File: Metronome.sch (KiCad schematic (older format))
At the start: 30 parts, among them CON1 PDI_50mil, IC1 ATXMEGA8E5-MU, P1 USB_B, Q1 Q_PMOS_GSD, U1 AS1117, U2 NCP706A

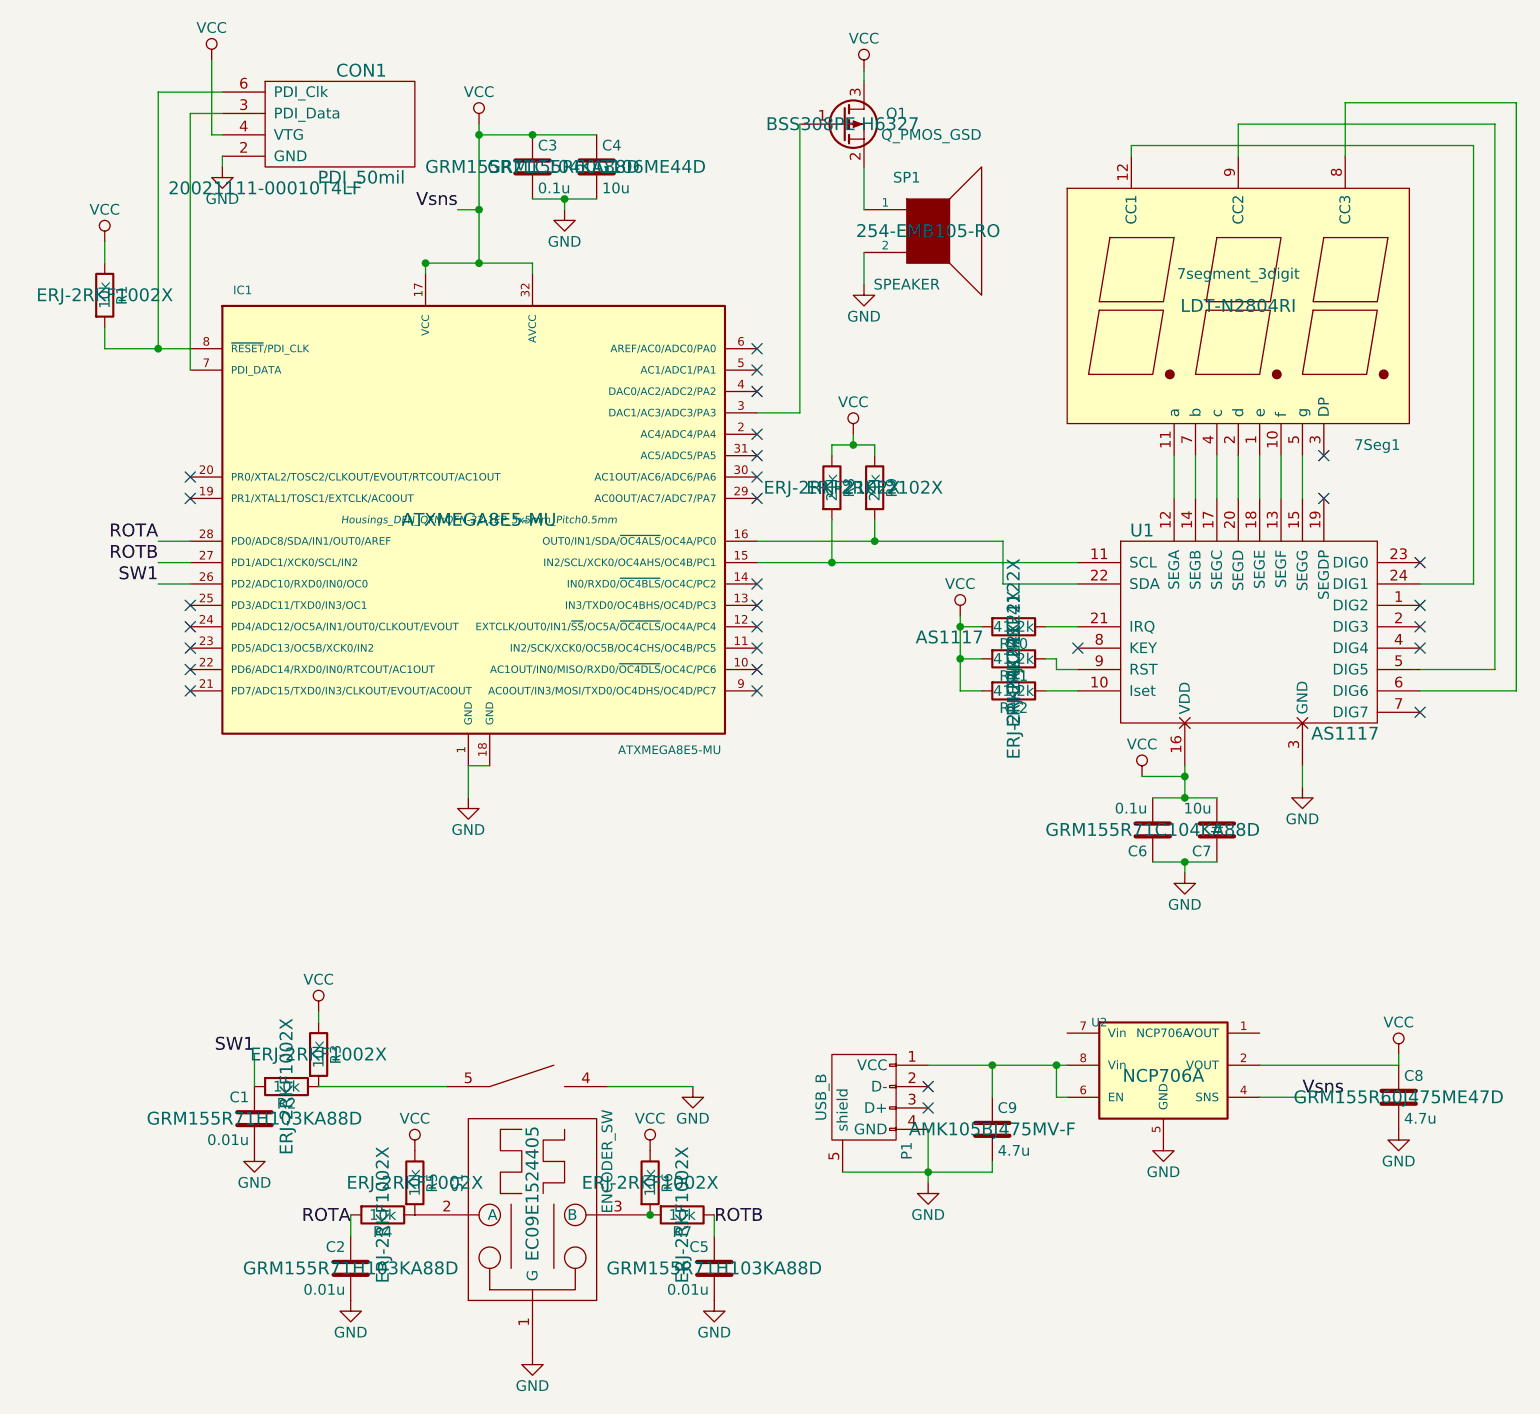
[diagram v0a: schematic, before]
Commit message: Hide footprints and MFP fields in schematic.
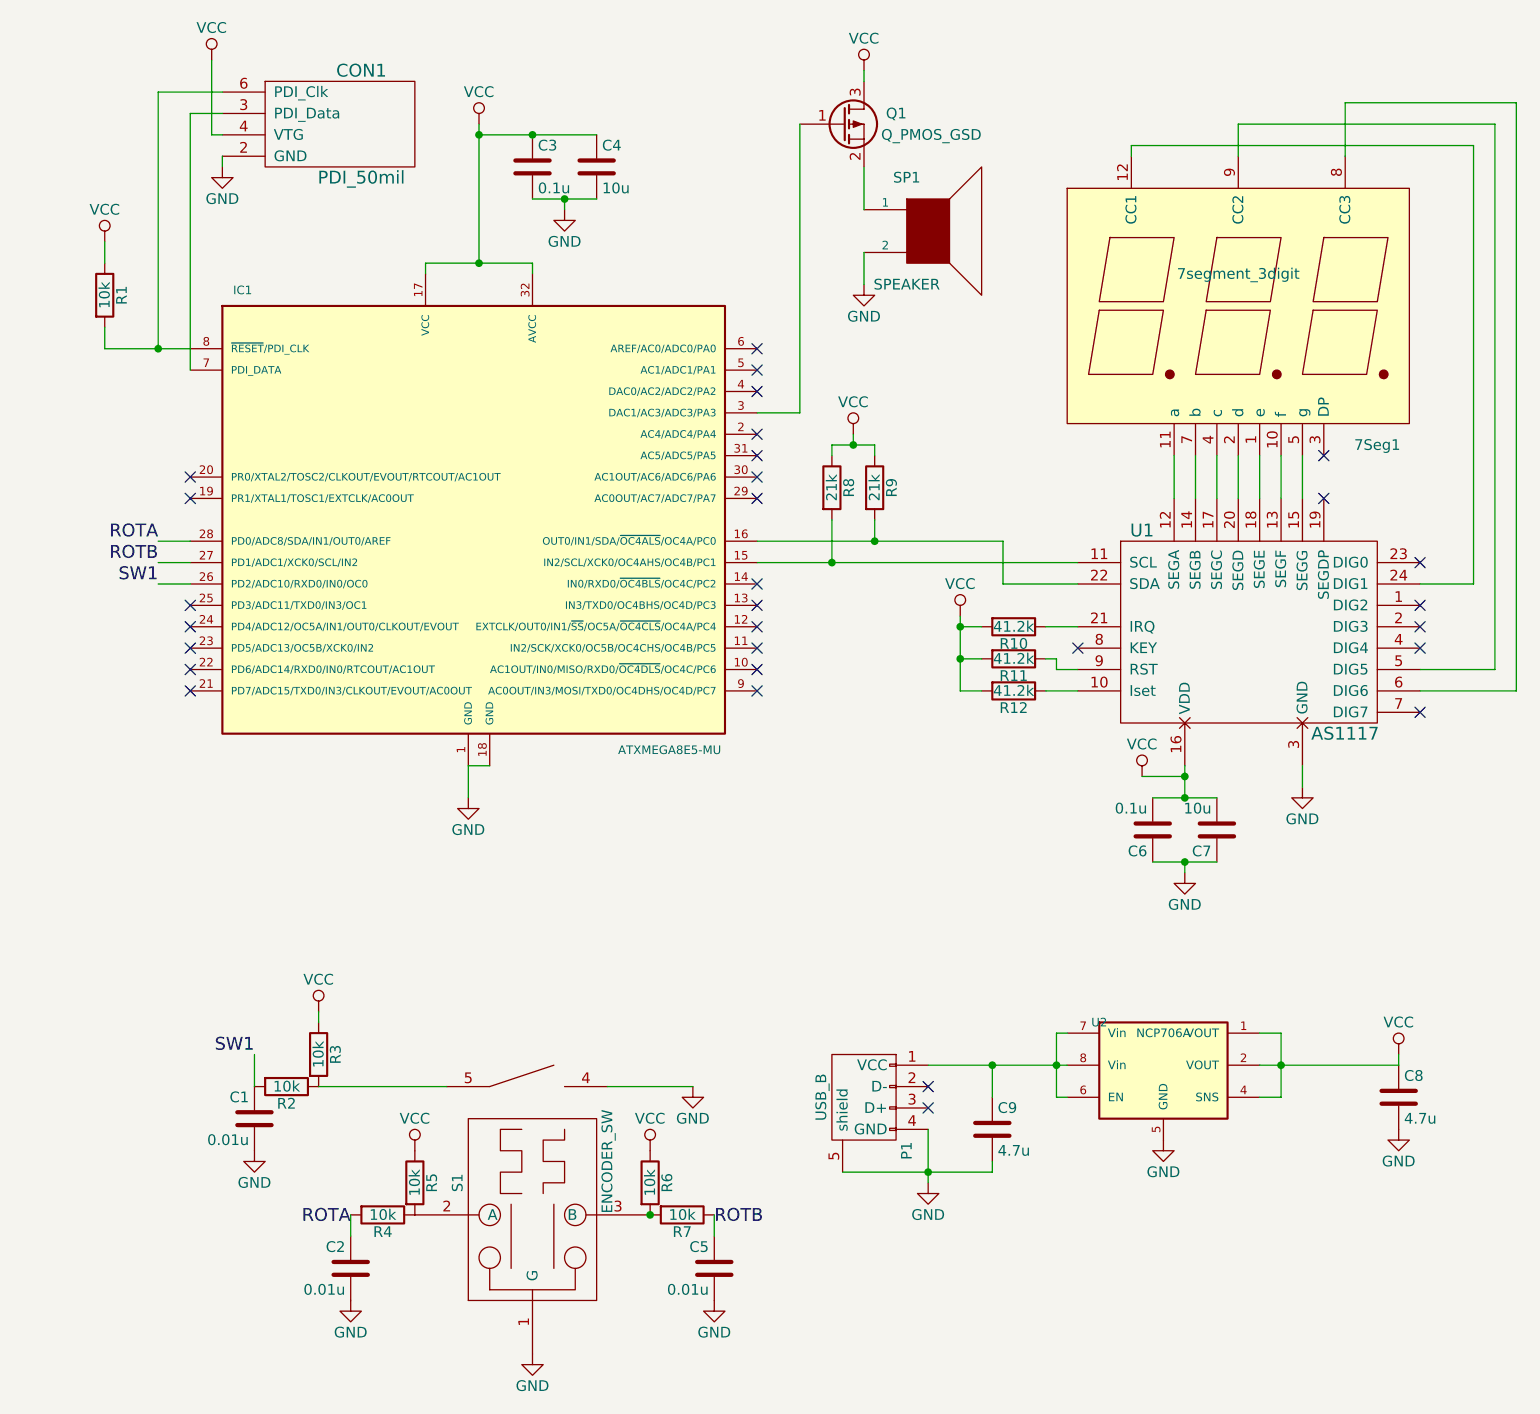
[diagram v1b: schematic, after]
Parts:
- C7: MFP # -> GRM155R60G106ME44D
- P1: MFN (none) -> FCI; MFP (none) -> 10118192-0001LF
- U1: MFP AS1117 -> AS1117-BQFT
- U2: MFP NCP706A -> NCP706AMX300TAG
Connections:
- net VCC: now also U2.1 (VOUT)
- net at C9.1, P1.1 (VCC), U2.6 (EN)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: now also U2.7 (Vin)
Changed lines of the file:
@@
 EESchema Schematic File Version 2
+LIBS:power
+LIBS:device
+LIBS:transistors
+LIBS:conn
+LIBS:linear
+LIBS:regul
+LIBS:74xx
+LIBS:cmos4000
+LIBS:adc-dac
+LIBS:memory
+LIBS:xilinx
+LIBS:microcontrollers
+LIBS:dsp
+LIBS:microchip
+LIBS:analog_switches
+LIBS:motorola
+LIBS:texas
+LIBS:intel
+LIBS:audio
+LIBS:interface
+LIBS:digital-audio
+LIBS:philips
+LIBS:display
+LIBS:cypress
+LIBS:siliconi
+LIBS:opto
+LIBS:atmel
+LIBS:contrib
+LIBS:valves
 LIBS:ams
 LIBS:encoder
@@
 LIBS:7segment_3digits
 LIBS:pdi_50mil
+LIBS:74xgxx
+LIBS:ac-dc
+LIBS:actel
+LIBS:Altera
+LIBS:analog_devices
+LIBS:brooktre
+LIBS:cmos_ieee
+LIBS:dc-dc
+LIBS:diode
+LIBS:elec-unifil
+LIBS:ESD_Protection
+LIBS:ftdi
+LIBS:gennum
+LIBS:graphic
+LIBS:hc11
+LIBS:ir
+LIBS:Lattice
+LIBS:logo
+LIBS:maxim
+LIBS:microchip_dspic33dsc
+LIBS:microchip_pic10mcu
+LIBS:microchip_pic12mcu
+LIBS:microchip_pic16mcu
+LIBS:microchip_pic18mcu
+LIBS:microchip_pic32mcu
+LIBS:motor_drivers
+LIBS:msp430
+LIBS:nordicsemi
+LIBS:nxp_armmcu
+LIBS:onsemi
+LIBS:Oscillators
+LIBS:powerint
+LIBS:Power_Management
+LIBS:pspice
+LIBS:references
+LIBS:relays
+LIBS:rfcom
+LIBS:sensors
+LIBS:silabs
+LIBS:stm8
+LIBS:stm32
+LIBS:supertex
+LIBS:switches
+LIBS:transf
+LIBS:ttl_ieee
+LIBS:video
+LIBS:Xicor
+LIBS:Zilog
 LIBS:Metronome-cache
 EELAYER 25 0
@@
 F 0 "IC1" H 1350 4250 40  0000 L BNN
 F 1 "ATXMEGA8E5-MU" H 3150 2100 40  0000 L BNN
-F 2 "Housings_DFN_QFN:QFN-32-1EP_5x5mm_Pitch0.5mm" H 2500 3200 35  0000 C CIN
+F 2 "Housings_DFN_QFN:QFN-32-1EP_5x5mm_Pitch0.5mm" H 2500 3200 35  0001 C CIN
 F 3 "" H 2500 3200 60  0000 C CNN
 F 4 "Atmel" H 2500 3200 60  0001 C CNN "MFN"
-F 5 "ATXMEGA8E5-MU" H 2500 3200 60  0000 C CNN "MFP"
+F 5 "ATXMEGA8E5-MU" H 2500 3200 60  0001 C CNN "MFP"
 	1    2500 3200
 	1    0    0    -1
@@
 F 3 "" H 750 2150 30  0000 C CNN
 F 4 "Panasonic" H 750 2150 60  0001 C CNN "MFN"
-F 5 "ERJ-2RKF1002X" H 750 2150 60  0000 C CNN "MFP"
+F 5 "ERJ-2RKF1002X" H 750 2150 60  0001 C CNN "MFP"
 	1    750  2150
 	1    0    0    -1
@@
 F 3 "" H 4700 3750 60  0000 C CNN
 F 4 "AMS" H 4700 3750 60  0001 C CNN "MFN"
-F 5 "AS1117" H 4700 3750 60  0000 C CNN "MFP"
+F 5 "AS1117-BQFT" H 4700 3750 60  0001 C CNN "MFP"
 	1    4700 3750
 	1    0    0    -1
@@
 F 3 "" H 5650 4650 60  0000 C CNN
 F 4 "Murata" H 5650 4650 60  0001 C CNN "MFN"
-F 5 "GRM155R71C104KA88D" H 5650 4650 60  0000 C CNN "MFP"
+F 5 "GRM155R71C104KA88D" H 5650 4650 60  0001 C CNN "MFP"
 	1    5650 4650
 	-1   0    0    1
@@
 F 3 "" H 5950 4650 60  0000 C CNN
 F 4 "Murata" H 5950 4650 60  0001 C CNN "MFN"
-F 5 "#" H 5950 4650 60  0000 C CNN "MFP"
+F 5 "GRM155R60G106ME44D" H 5950 4650 60  0001 C CNN "MFP"
 	1    5950 4650
 	-1   0    0    1
@@
 F 3 "" H 5000 3700 30  0000 C CNN
 F 4 "Panasonic" H 5000 3700 60  0001 C CNN "MFN"
-F 5 "ERJ-2RKF4122X" H 5000 3700 60  0000 C CNN "MFP"
+F 5 "ERJ-2RKF4122X" H 5000 3700 60  0001 C CNN "MFP"
 	1    5000 3700
 	0    1    1    0
@@
 F 3 "" H 2750 1550 60  0000 C CNN
 F 4 "Murata" H 2750 1550 60  0001 C CNN "MFN"
-F 5 "GRM155R71C104KA88D" H 2750 1550 60  0000 C CNN "MFP"
+F 5 "GRM155R71C104KA88D" H 2750 1550 60  0001 C CNN "MFP"
 	1    2750 1550
 	1    0    0    -1
@@
 F 3 "" H 3050 1550 60  0000 C CNN
 F 4 "Murata" H 3050 1550 60  0001 C CNN "MFN"
-F 5 "GRM155R60G106ME44D" H 3050 1550 60  0000 C CNN "MFP"
+F 5 "GRM155R60G106ME44D" H 3050 1550 60  0001 C CNN "MFP"
 	1    3050 1550
 	1    0    0    -1
@@
 F 3 "" H 4150 3050 30  0000 C CNN
 F 4 "Panasonic" H 4150 3050 60  0001 C CNN "MFN"
-F 5 "ERJ-2RKF2102X" H 4150 3050 60  0000 C CNN "MFP"
+F 5 "ERJ-2RKF2102X" H 4150 3050 60  0001 C CNN "MFP"
 	1    4150 3050
 	1    0    0    -1
@@
 Wire Wire Line
 	2750 2000 2750 2050
-Connection ~ 2250 2000
 Wire Wire Line
 	2500 1400 3050 1400
@@
 F 3 "" H 2750 6350 60  0000 C CNN
 F 4 "Alps" H 2750 6350 60  0001 C CNN "MFN"
-F 5 "EC09E1524405" H 2750 6350 60  0000 C CNN "MFP"
+F 5 "EC09E1524405" H 2750 6350 60  0001 C CNN "MFP"
 	1    2750 6350
 	0    -1   -1   0
@@
 F 3 "" H 1450 6000 60  0000 C CNN
 F 4 "Murata" H 1450 6000 60  0001 C CNN "MFN"
-F 5 "GRM155R71H103KA88D" H 1450 6000 60  0000 C CNN "MFP"
+F 5 "GRM155R71H103KA88D" H 1450 6000 60  0001 C CNN "MFP"
 	1    1450 6000
 	-1   0    0    -1
@@
 F 3 "" H 5700 5800 60  0000 C CNN
 F 4 "On Semiconductor" H 5700 5800 60  0001 C CNN "MFN"
-F 5 "NCP706A" H 5700 5800 60  0000 C CNN "MFP"
+F 5 "NCP706AMX300TAG" H 5700 5800 60  0001 C CNN "MFP"
 	1    5700 5800
 	1    0    0    -1
@@
 F 3 "" H 6800 5900 60  0000 C CNN
 F 4 "Murata" H 6800 5900 60  0001 C CNN "MFN"
-F 5 "GRM155R60J475ME47D" H 6800 5900 60  0000 C CNN "MFP"
+F 5 "GRM155R60J475ME47D" H 6800 5900 60  0001 C CNN "MFP"
 	1    6800 5900
 	1    0    0    -1
@@
 F 3 "" H 5800 2200 60  0000 C CNN
 F 4 "Lumex" H 6050 2200 60  0001 C CNN "MFN"
-F 5 "LDT-N2804RI" H 6050 2200 60  0000 C CNN "MFP"
+F 5 "LDT-N2804RI" H 6050 2200 60  0001 C CNN "MFP"
 	1    6050 2200
 	1    0    0    -1
@@
 NoConn ~ 1150 3900
 NoConn ~ 1150 4000
-Text Label 6350 5900 0    60   ~ 0
-Vsns
-Wire Wire Line
-	6350 5900 6150 5900
-Text Label 2400 1750 2    60   ~ 0
-Vsns
-Wire Wire Line
-	2400 1750 2500 1750
-Connection ~ 2500 1750
 Wire Wire Line
 	7150 3500 6900 3500
@@
 F 3 "" H 1500 1650 60  0000 C CNN
 F 4 "FCI" H 1500 1650 60  0001 C CNN "MFN"
-F 5 "20021111-00010T4LF" H 1500 1650 60  0000 C CNN "MFP"
+F 5 "20021111-00010T4LF" H 1500 1650 60  0001 C CNN "MFP"
 	1    1500 1650
 	1    0    0    -1
@@
 F 3 "" H 4600 1850 60  0000 C CNN
 F 4 "Kobitone" H 4600 1850 60  0001 C CNN "MFN"
-F 5 "254-EMB105-RO" H 4600 1850 60  0000 C CNN "MFP"
+F 5 "254-EMB105-RO" H 4600 1850 60  0001 C CNN "MFP"
 	1    4600 1850
 	1    0    0    -1
@@
 F 3 "" H 4200 1350 60  0000 C CNN
 F 4 "Infineon" H 4200 1350 60  0001 C CNN "MFN"
-F 5 "BSS308PE H6327" H 4200 1350 60  0000 C CNN "MFP"
+F 5 "BSS308PE H6327" H 4200 1350 60  0001 C CNN "MFP"
 	1    4200 1350
 	1    0    0    -1
@@
 F 2 "Connect:USB_Micro-B" V 4250 5850 60  0001 C CNN
 F 3 "" V 4250 5850 60  0000 C CNN
+F 4 "FCI" H 4300 5950 60  0001 C CNN "MFN"
+F 5 "10118192-0001LF" H 4300 5950 60  0001 C CNN "MFP"
 	1    4300 5950
 	0    -1   1    0
@@
 	4600 5750 5250 5750
 Wire Wire Line
-	5200 5750 5200 5900
+	5200 5600 5200 5900
 Wire Wire Line
 	5200 5900 5250 5900
@@
 F 3 "" H 4900 6050 60  0000 C CNN
 F 4 "~" H 4900 6050 60  0001 C CNN "MFN"
-F 5 "AMK105BJ475MV-F" H 4900 6050 60  0000 C CNN "MFP"
+F 5 "AMK105BJ475MV-F" H 4900 6050 60  0001 C CNN "MFP"
 	1    4900 6050
 	1    0    0    -1
@@
 F 3 "" H 5000 3850 30  0000 C CNN
 F 4 "Panasonic" H 5000 3850 60  0001 C CNN "MFN"
-F 5 "ERJ-2RKF4122X" H 5000 3850 60  0000 C CNN "MFP"
+F 5 "ERJ-2RKF4122X" H 5000 3850 60  0001 C CNN "MFP"
 	1    5000 3850
 	0    1    1    0
@@
 F 3 "" H 5000 4000 30  0000 C CNN
 F 4 "Panasonic" H 5000 4000 60  0001 C CNN "MFN"
-F 5 "ERJ-2RKF4122X" H 5000 4000 60  0000 C CNN "MFP"
+F 5 "ERJ-2RKF4122X" H 5000 4000 60  0001 C CNN "MFP"
 	1    5000 4000
 	0    1    1    0
@@
 F 3 "" H 4350 3050 30  0000 C CNN
 F 4 "Panasonic" H 4350 3050 60  0001 C CNN "MFN"
-F 5 "ERJ-2RKF2102X" H 4350 3050 60  0000 C CNN "MFP"
+F 5 "ERJ-2RKF2102X" H 4350 3050 60  0001 C CNN "MFP"
 	1    4350 3050
 	1    0    0    -1
@@
 F 3 "" H 3300 6300 30  0000 C CNN
 F 4 "Panasonic" H 3300 6300 60  0001 C CNN "MFN"
-F 5 "ERJ-2RKF1002X" H 3300 6300 60  0000 C CNN "MFP"
+F 5 "ERJ-2RKF1002X" H 3300 6300 60  0001 C CNN "MFP"
 	1    3300 6300
 	1    0    0    -1
@@
 F 3 "" H 3450 6450 30  0000 C CNN
 F 4 "Panasonic" H 3450 6450 60  0001 C CNN "MFN"
-F 5 "ERJ-2RKF1002X" H 3450 6450 60  0000 C CNN "MFP"
+F 5 "ERJ-2RKF1002X" H 3450 6450 60  0001 C CNN "MFP"
 	1    3450 6450
 	0    1    1    0
@@
 F 3 "" H 2200 6300 30  0000 C CNN
 F 4 "Panasonic" H 2200 6300 60  0001 C CNN "MFN"
-F 5 "ERJ-2RKF1002X" H 2200 6300 60  0000 C CNN "MFP"
+F 5 "ERJ-2RKF1002X" H 2200 6300 60  0001 C CNN "MFP"
 	1    2200 6300
 	1    0    0    -1
@@
 F 3 "" H 2050 6450 30  0000 C CNN
 F 4 "Panasonic" H 2050 6450 60  0001 C CNN "MFN"
-F 5 "ERJ-2RKF1002X" H 2050 6450 60  0000 C CNN "MFP"
+F 5 "ERJ-2RKF1002X" H 2050 6450 60  0001 C CNN "MFP"
 	1    2050 6450
 	0    1    1    0
@@
 F 3 "" H 1750 5700 30  0000 C CNN
 F 4 "Panasonic" H 1750 5700 60  0001 C CNN "MFN"
-F 5 "ERJ-2RKF1002X" H 1750 5700 60  0000 C CNN "MFP"
+F 5 "ERJ-2RKF1002X" H 1750 5700 60  0001 C CNN "MFP"
 	1    1750 5700
 	1    0    0    -1
@@
 F 3 "" H 1600 5850 30  0000 C CNN
 F 4 "Panasonic" H 1600 5850 60  0001 C CNN "MFN"
-F 5 "ERJ-2RKF1002X" H 1600 5850 60  0000 C CNN "MFP"
+F 5 "ERJ-2RKF1002X" H 1600 5850 60  0001 C CNN "MFP"
 	1    1600 5850
 	0    1    1    0
@@
 F 3 "" H 1900 6700 60  0000 C CNN
 F 4 "Murata" H 1900 6700 60  0001 C CNN "MFN"
-F 5 "GRM155R71H103KA88D" H 1900 6700 60  0000 C CNN "MFP"
+F 5 "GRM155R71H103KA88D" H 1900 6700 60  0001 C CNN "MFP"
 	1    1900 6700
 	-1   0    0    -1
@@
 F 3 "" H 3600 6700 60  0000 C CNN
 F 4 "Murata" H 3600 6700 60  0001 C CNN "MFN"
-F 5 "GRM155R71H103KA88D" H 3600 6700 60  0000 C CNN "MFP"
+F 5 "GRM155R71H103KA88D" H 3600 6700 60  0001 C CNN "MFP"
 	1    3600 6700
 	-1   0    0    -1
@@
 NoConn ~ 6450 2900
 NoConn ~ 6450 3100
+Wire Wire Line
+	5250 5600 5200 5600
+Wire Wire Line
+	6150 5600 6250 5600
+Wire Wire Line
+	6250 5600 6250 5900
+Connection ~ 6250 5750
+Wire Wire Line
+	6250 5900 6150 5900
 $EndSCHEMATC
